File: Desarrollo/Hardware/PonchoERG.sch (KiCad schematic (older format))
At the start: 1 part

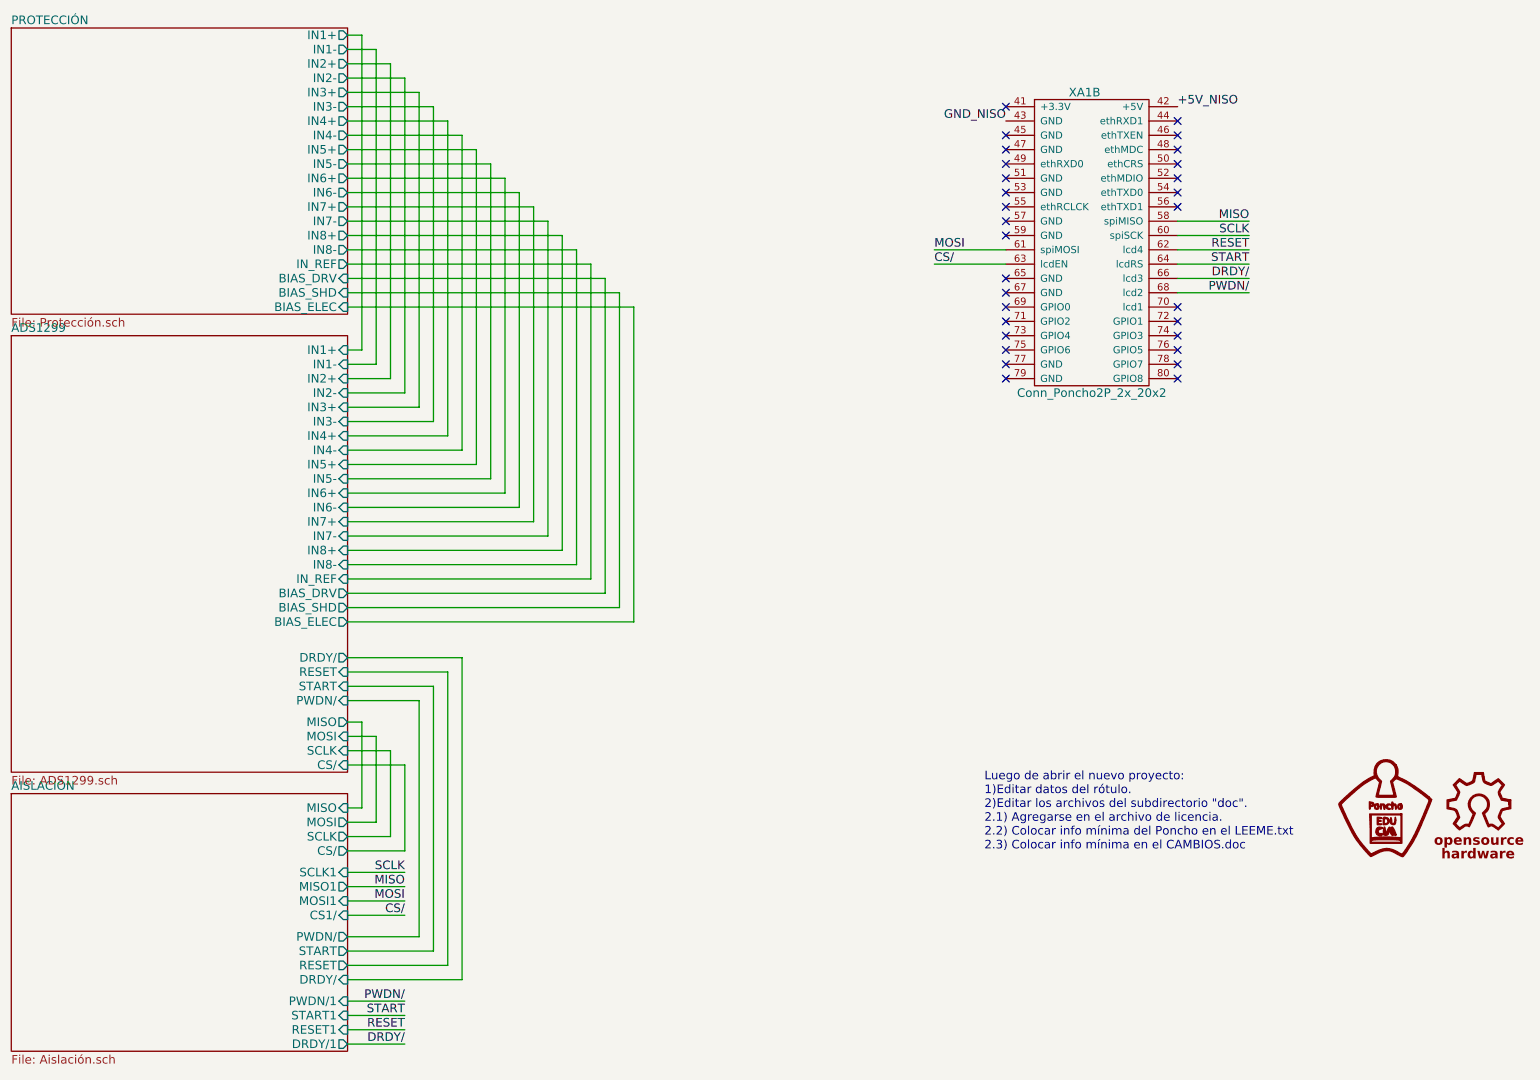
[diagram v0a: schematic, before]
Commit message: Última actualización de ruteo. Redimensión de placa. Cambio de ancho de algunas pistas. Cambio de componentes. Agregado de inductancias de aislación de masas y alimentación +5V.
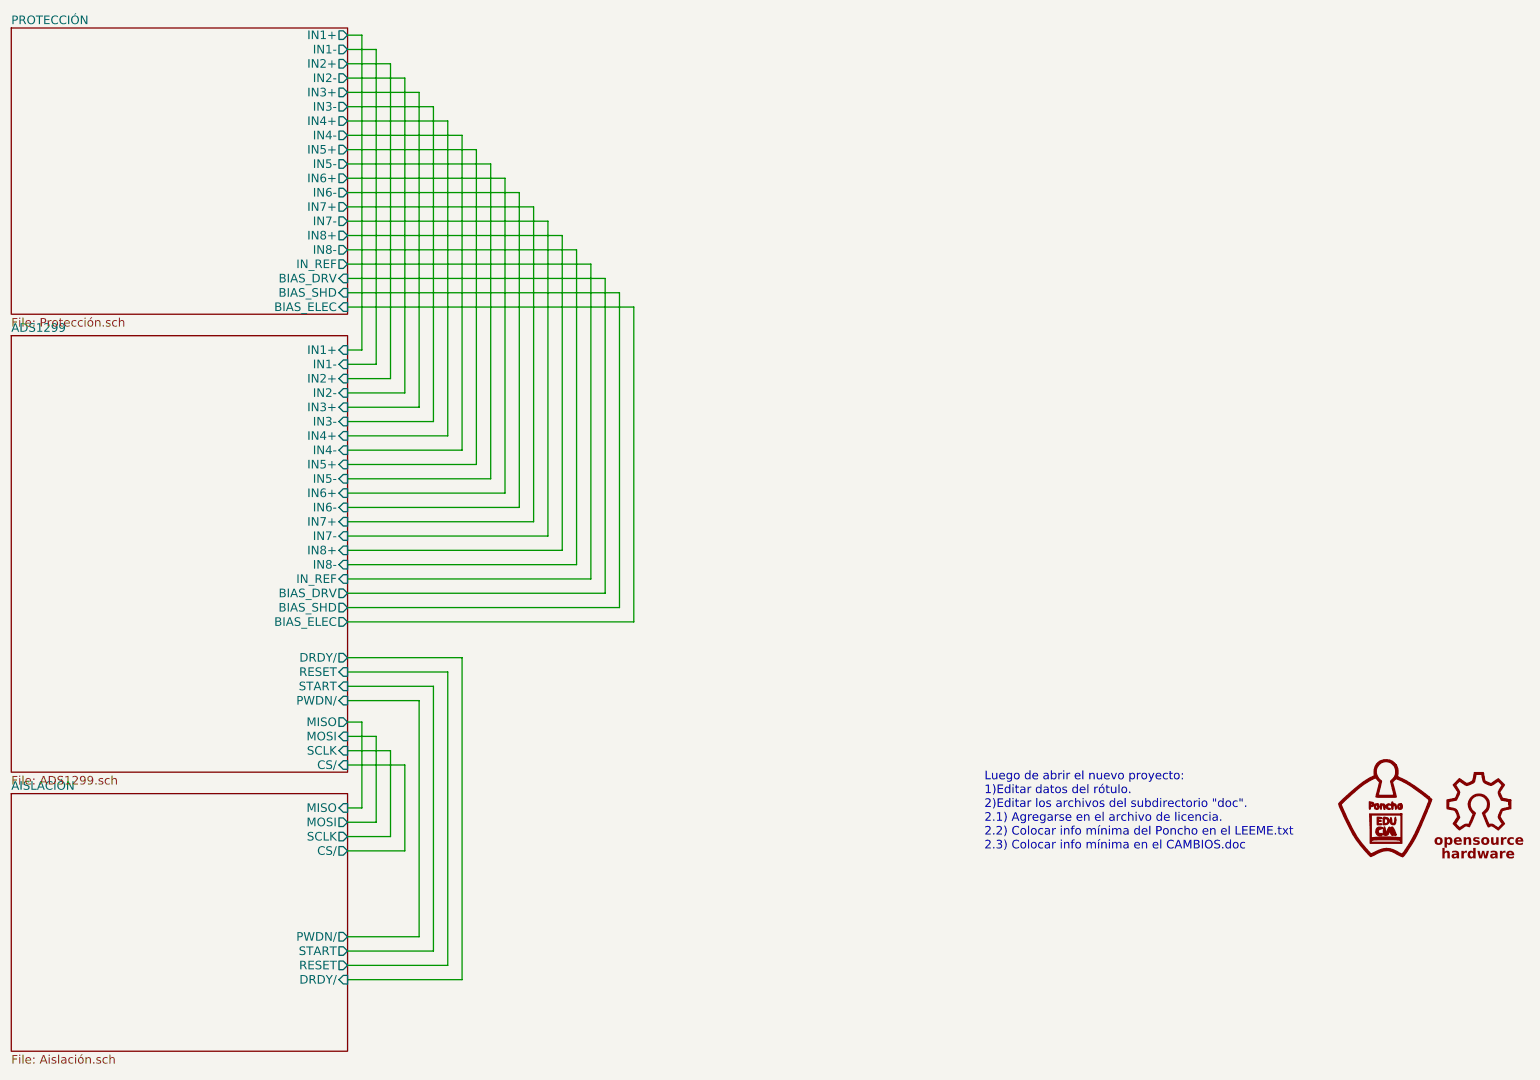
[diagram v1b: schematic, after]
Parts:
- removed XA1: Conn_Poncho2P_2x_20x2, Poncho_Esqueleto:Conn_Poncho_Izquierdo, symbol Conn_Poncho2P_2x_20x2
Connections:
- no-connect marks 30 -> 0
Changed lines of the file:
@@
 F29 "RESET" I R 2900 5050 60
-$EndSheet
-$Sheet
-S 550  5900 2350 1800
-U 57BDC3A8
-F0 "AISLACIÓN" 60
-F1 "Aislación.sch" 60
-F2 "MISO" I R 2900 6000 60
-F3 "MOSI" O R 2900 6100 60
-F4 "SCLK" O R 2900 6200 60
-F5 "CS/" O R 2900 6300 60
-F6 "START1" I R 2900 7450 60
-F7 "RESET1" I R 2900 7550 60
-F8 "DRDY/1" O R 2900 7650 60
-F9 "RESET" O R 2900 7100 60
-F10 "START" O R 2900 7000 60
-F11 "DRDY/" I R 2900 7200 60
-F12 "MISO1" O R 2900 6550 60
-F13 "MOSI1" I R 2900 6650 60
-F14 "SCLK1" I R 2900 6450 60
-F15 "CS1/" I R 2900 6750 60
-F16 "PWDN/1" I R 2900 7350 60
-F17 "PWDN/" O R 2900 6900 60
 $EndSheet
 Wire Wire Line
@@
 Wire Wire Line
 	4600 4400 2900 4400
-$Comp
-L Conn_Poncho2P_2x_20x2 XA1
-U 2 1 57CB029C
-P 7750 1400
-F 0 "XA1" H 8050 1800 60  0000 C CNN
-F 1 "Conn_Poncho2P_2x_20x2" H 8100 -300 60  0000 C CNN
-F 2 "Poncho_Esqueleto:Conn_Poncho_Izquierdo" H 7750 1400 60  0001 C CNN
-F 3 "" H 7750 1400 60  0000 C CNN
-	2    7750 1400
-	1    0    0    -1
-$EndComp
-Text Label 8700 1100 0    60   ~ 0
-+5V_NISO
-Text Label 7500 1200 2    60   ~ 0
-GND_NISO
-Wire Wire Line
-	8700 1900 9200 1900
-Wire Wire Line
-	7500 2100 7000 2100
-Wire Wire Line
-	8700 2100 9200 2100
-Wire Wire Line
-	7500 2200 7000 2200
-Wire Wire Line
-	8700 2200 9200 2200
-Wire Wire Line
-	8700 2300 9200 2300
-Text Label 9200 1900 2    60   ~ 0
-MISO
-Text Label 9200 2000 2    60   ~ 0
-SCLK
-Text Label 9200 2100 2    60   ~ 0
-RESET
-Text Label 9200 2200 2    60   ~ 0
-START
-Text Label 7000 2200 0    60   ~ 0
-CS/
-Text Label 7000 2100 0    60   ~ 0
-MOSI
-Text Label 9200 2300 2    60   ~ 0
-DRDY/
-Wire Wire Line
-	2900 6550 3300 6550
-Wire Wire Line
-	2900 6650 3300 6650
-Wire Wire Line
-	2900 6750 3300 6750
-Wire Wire Line
-	2900 7450 3300 7450
-Wire Wire Line
-	2900 7550 3300 7550
-Wire Wire Line
-	2900 7650 3300 7650
-Text Label 3300 6450 2    60   ~ 0
-SCLK
-Text Label 3300 6550 2    60   ~ 0
-MISO
-Text Label 3300 6650 2    60   ~ 0
-MOSI
-Text Label 3300 6750 2    60   ~ 0
-CS/
-Text Label 3300 7450 2    60   ~ 0
-START
-Text Label 3300 7550 2    60   ~ 0
-RESET
-Text Label 3300 7650 2    60   ~ 0
-DRDY/
-NoConn ~ 7500 1100
-NoConn ~ 7500 1300
-NoConn ~ 7500 1400
-NoConn ~ 7500 1500
-NoConn ~ 7500 1600
-NoConn ~ 7500 1700
-NoConn ~ 7500 1800
-NoConn ~ 7500 1900
-NoConn ~ 7500 2000
-NoConn ~ 7500 2300
-NoConn ~ 7500 2400
-NoConn ~ 7500 2500
-NoConn ~ 7500 2600
-NoConn ~ 7500 2700
-NoConn ~ 7500 2800
-NoConn ~ 7500 2900
-NoConn ~ 7500 3000
-NoConn ~ 8700 3000
-NoConn ~ 8700 2900
-NoConn ~ 8700 2800
-NoConn ~ 8700 2700
-NoConn ~ 8700 2600
-NoConn ~ 8700 2500
-NoConn ~ 8700 1800
-NoConn ~ 8700 1700
-NoConn ~ 8700 1600
-NoConn ~ 8700 1500
-NoConn ~ 8700 1400
-NoConn ~ 8700 1300
-NoConn ~ 8700 1200
 Wire Wire Line
 	3400 6900 2900 6900
@@
 Wire Wire Line
 	2900 7200 3700 7200
-Wire Wire Line
-	2900 7350 3300 7350
-Text Label 3300 7350 2    60   ~ 0
-PWDN/
-Wire Wire Line
-	8700 2400 9200 2400
-Text Label 9200 2400 2    60   ~ 0
-PWDN/
 Wire Wire Line
 	3000 6000 3000 5400
@@
 Wire Wire Line
 	3300 5700 3300 6300
-Wire Wire Line
-	2900 6450 3300 6450
-Wire Wire Line
-	9200 2000 8700 2000
 Wire Wire Line
 	2900 5250 3400 5250
@@
 Wire Wire Line
 	4900 4700 2900 4700
+$Sheet
+S 550  5900 2350 1800
+U 57BDC3A8
+F0 "AISLACIÓN" 60
+F1 "Aislación.sch" 60
+F2 "MISO" I R 2900 6000 60
+F3 "MOSI" O R 2900 6100 60
+F4 "SCLK" O R 2900 6200 60
+F5 "CS/" O R 2900 6300 60
+F6 "RESET" O R 2900 7100 60
+F7 "START" O R 2900 7000 60
+F8 "DRDY/" I R 2900 7200 60
+F9 "PWDN/" O R 2900 6900 60
+$EndSheet
 $EndSCHEMATC

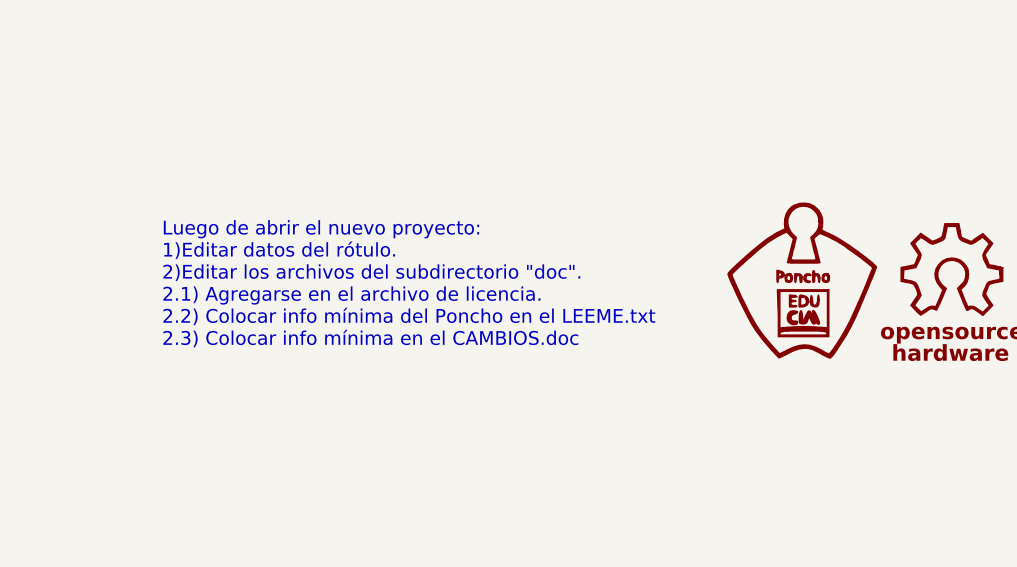
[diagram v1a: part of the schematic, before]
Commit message: Actualización de esquemático, se completaron campos de "Hoja de dato" y "Código Digikey" para cada componente. Se completaron los rótulos de hojas. Versión Final de PCB. Actualización de tamaño de pistas y redimensión de zonas de relleno. Lista de Materiales actualizada en carpeta "Documentación".
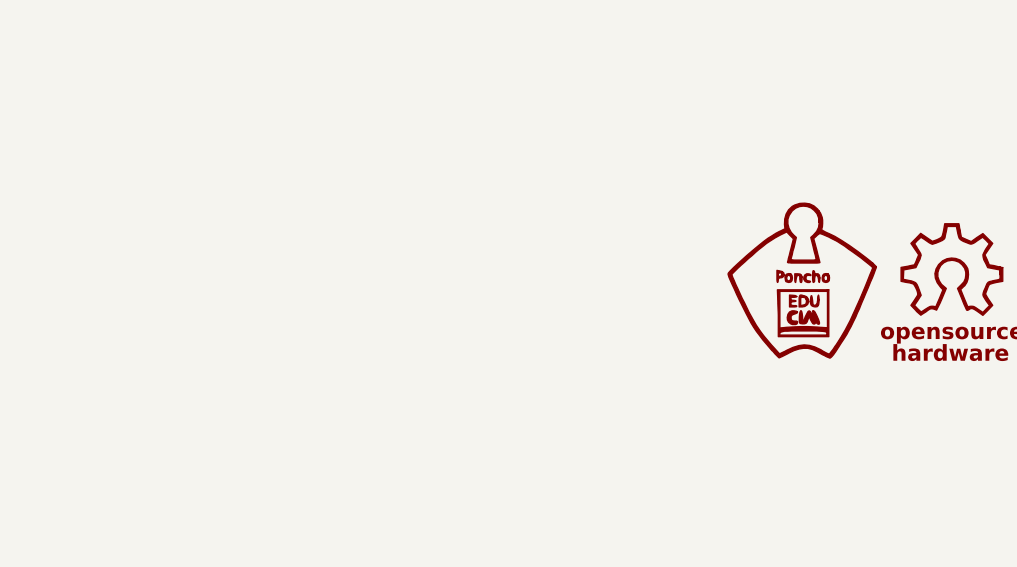
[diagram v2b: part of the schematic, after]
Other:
- note removed: "Luego de abrir el nuevo proyecto:\n1)Editar datos del rótulo.\n2)Editar los archivos del subdirectorio "doc".\n2.1) Agregarse en el archivo de licencia.\n2.2) Colocar info mínima del Poncho en el LEEME.txt\n2.3) Colocar info mínima en el CAMBIOS.doc"
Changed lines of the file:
@@
 encoding utf-8
 Sheet 1 4
-Title "Poncho Mediano - Modelo - Ejemplo - Template"
+Title "Poncho de Adquisición de Biopotenciales"
 Date "lun 05 oct 2015"
 Rev "1.0"
-Comp "Bruno Javier Cesario"
-Comment1 "https://github.com/ciaa/Ponchos/tree/master/modelos/doc"
+Comp "FIUNER"
+Comment1 "https://github.com/bcesario/ERG-Developers.git"
 Comment2 "Autores y Licencia del template (Diego Brengi - UNLaM)"
-Comment3 "Autor del poncho (COMPLETAR NOMBRE Y APELLIDO). Ver directorio \"doc\""
-Comment4 "CÓDIGO PONCHO:"
+Comment3 "Bruno Javier Cesario"
+Comment4 ""
 $EndDescr
 $Comp
@@
 	1    0    0    -1
 $EndComp
-Text Notes 7350 6300 0    60   ~ 0
-Luego de abrir el nuevo proyecto:\n1)Editar datos del rótulo.\n2)Editar los archivos del subdirectorio "doc".\n2.1) Agregarse en el archivo de licencia.\n2.2) Colocar info mínima del Poncho en el LEEME.txt\n2.3) Colocar info mínima en el CAMBIOS.doc
 $Sheet
 S 550  550  2350 2000
